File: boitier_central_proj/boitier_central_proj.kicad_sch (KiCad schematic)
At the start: 1 part, among them U1 XIAO-nRF52840-SMD

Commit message: PCB V1
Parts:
- added D1: 1N5819, Diode_THT:D_DO-41_SOD81_P10.16mm_Horizontal, symbol Diode:1N5819
- added D2: LED, LED_THT:LED_D5.0mm, symbol Device:LED
- added J1, J4: Conn_01x02_Pin, Connector_JST:JST_XH_B2B-XH-A_1x02_P2.50mm_Vertical, symbol Connector:Conn_01x02_Pin
- added J2: Conn_01x03_Pin, Connector_JST:JST_XH_B3B-XH-A_1x03_P2.50mm_Vertical, symbol Connector:Conn_01x03_Pin
- added Q1: IRLZ34N, Package_TO_SOT_THT:TO-220-3_Vertical, symbol Transistor_FET:IRLZ34N
- added R1, R2: 1k, Resistor_THT:R_Axial_DIN0204_L3.6mm_D1.6mm_P2.54mm_Vertical, symbol Device:R
- added S1, S2: JS102011SAQN, Button_Switch_SMD:SW_SPDT_CK_JS102011SAQN, symbol JS102011SAQN:JS102011SAQN
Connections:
- net leds_GND is gone; now on net GND: U1.13 (GND)
- net Arme_Selection: now reaches U1.1 (P0.02_A0_D0)
- net Arme_Selection: now also S2.2
- net 3V3: now reaches U1.12 (3V3)
- net 3V3: now also D1.1 (K), J1.2 (Pin_2), S2.1
- net moteur_c: now reaches U1.3 (P0.28_A2_D2)
- net moteur_c: now also R1.2
- net Out+ renamed BAT+
- net BAT+: now also D2.2 (A), S1.2
- net Out- renamed GND
- net GND: now also D2.1 (K), J2.2 (Pin_2), J4.2 (Pin_2), Q1.3 (S), R2.2, S1.1, S2.3
- net leds_5V renamed LEDS+
- net LEDS+: now also J2.3 (Pin_3)
- net leds_dig renamed LEDS_C
- net LEDS_C: now also J2.1 (Pin_1)
- new net: D1.2 (A), J1.1 (Pin_1), Q1.2 (D)
- new net: Q1.1 (G), R1.1, R2.1
- new net: J4.1 (Pin_1), S1.3
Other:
- note added: "Alimentation"
- note added: "Connection LEDs"
- note added: "Gestion Moteur"
- note added: "Selection Armes"

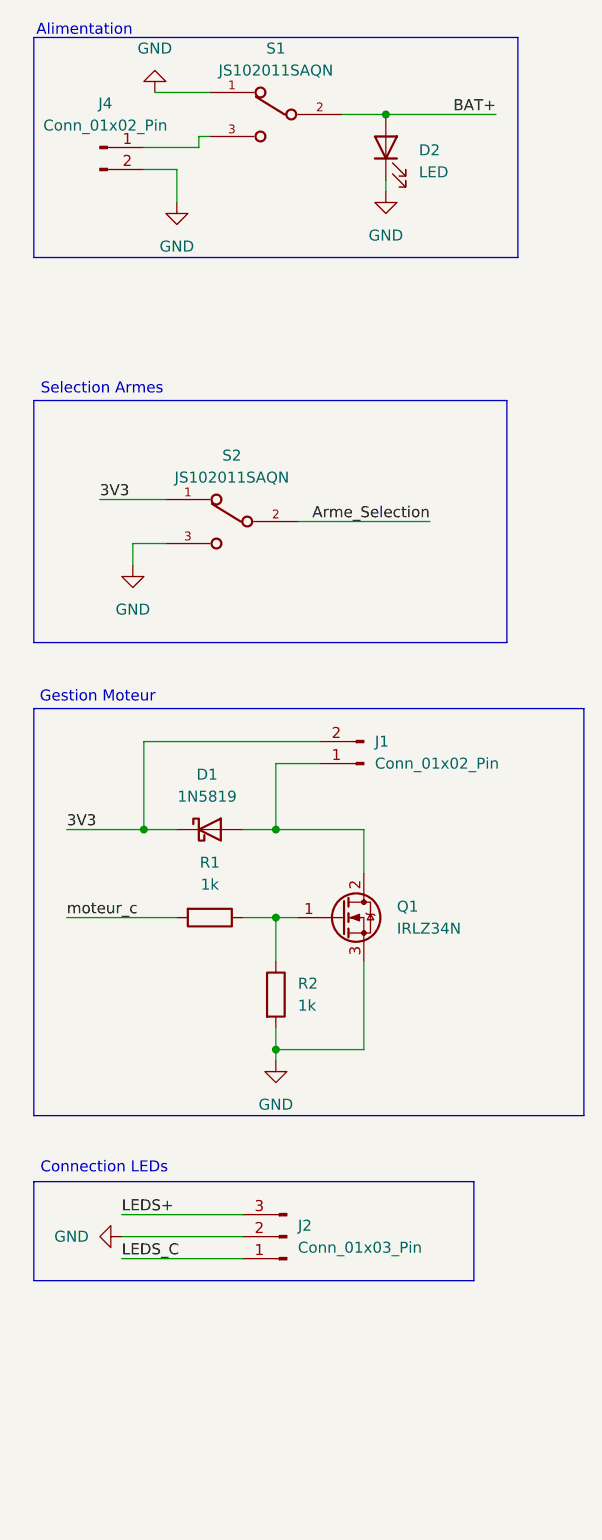
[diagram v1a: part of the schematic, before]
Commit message: Ajout du module TP4056 dans le schematic
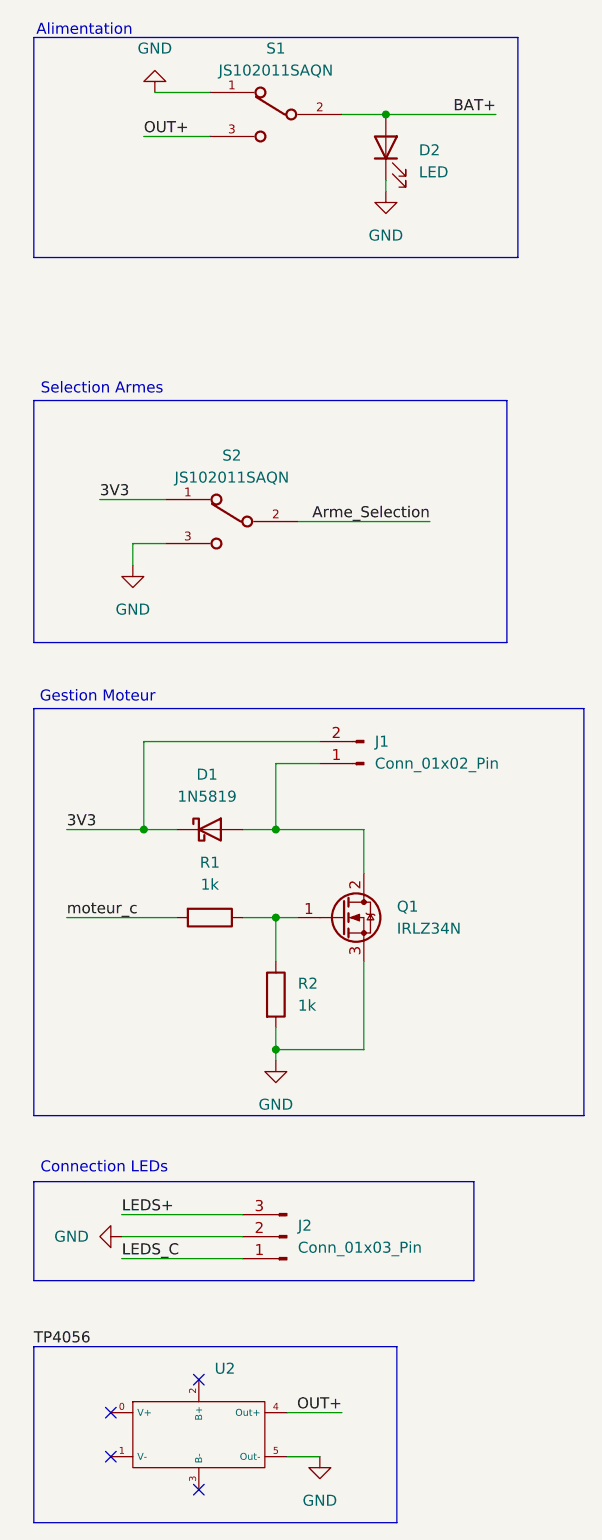
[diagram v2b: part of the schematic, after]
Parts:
- removed J4: Conn_01x02_Pin, Connector_JST:JST_XH_B2B-XH-A_1x02_P2.50mm_Vertical, symbol Connector:Conn_01x02_Pin
- added U2: ~, symbol TP4056_lib:TP4056_module
- S1, S2: footprint Button_Switch_SMD:SW_SPDT_CK_JS102011SAQN -> JS102011SAQN:SW_JS102011SAQN
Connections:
- net GND: now also U2.5 (Out-)
- net OUT+: now reaches S1.3
- net OUT+: now also U2.4 (Out+)
- no-connect marks 0 -> 4
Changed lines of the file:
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@@
 	(paper "A4")
+	(rectangle
+		(start 15.24 167.64)
+		(end 57.15 187.96)
+		(stroke
+			(width 0)
+			(type default)
+		)
+		(fill
+			(type none)
+		)
+	)
 	(rectangle
 		(start 15.24 148.59)
@@
 		(color 0 0 0 0)
 	)
+	(no_connect
+		(at 34.29 171.45)
+	)
+	(no_connect
+		(at 24.13 180.34)
+	)
+	(no_connect
+		(at 24.13 175.26)
+	)
+	(no_connect
+		(at 34.29 184.15)
+	)
 	(wire
 		(pts
@@
 	(wire
 		(pts
+			(xy 44.45 175.26) (xy 50.8 175.26)
+		)
+		(stroke
+			(width 0)
+			(type default)
+		)
+	)
+	(wire
+		(pts
 			(xy 48.26 100.33) (xy 43.18 100.33)
 		)
@@
 	(wire
 		(pts
-			(xy 34.29 27.94) (xy 35.56 27.94)
-		)
-		(stroke
-			(width 0)
-			(type default)
-		)
-	)
-	(wire
-		(pts
 			(xy 175.26 50.8) (xy 191.77 50.8)
 		)
@@
 	(wire
 		(pts
-			(xy 27.94 31.75) (xy 31.75 31.75)
-		)
-		(stroke
-			(width 0)
-			(type default)
-		)
-	)
-	(wire
-		(pts
 			(xy 53.34 133.35) (xy 43.18 133.35)
 		)
@@
 	(wire
 		(pts
+			(xy 44.45 180.34) (xy 48.26 180.34)
+		)
+		(stroke
+			(width 0)
+			(type default)
+		)
+	)
+	(wire
+		(pts
 			(xy 147.32 76.2) (xy 147.32 86.36)
 		)
@@
 	(wire
 		(pts
-			(xy 34.29 27.94) (xy 34.29 29.21)
-		)
-		(stroke
-			(width 0)
-			(type default)
-		)
-	)
-	(wire
-		(pts
 			(xy 115.57 50.8) (xy 133.35 50.8)
 		)
@@
 	(wire
 		(pts
-			(xy 34.29 29.21) (xy 27.94 29.21)
+			(xy 27.94 27.94) (xy 35.56 27.94)
 		)
 		(stroke
@@
 		(pts
 			(xy 26.67 74.93) (xy 26.67 77.47)
-		)
-		(stroke
-			(width 0)
-			(type default)
-		)
-	)
-	(wire
-		(pts
-			(xy 31.75 31.75) (xy 31.75 35.56)
 		)
 		(stroke
@@
 		)
 	)
+	(label "OUT+"
+		(at 50.8 175.26 180)
+		(effects
+			(font
+				(size 1.27 1.27)
+			)
+			(justify right bottom)
+		)
+	)
 	(label "BAT+"
 		(at 147.32 86.36 90)
@@
 		)
 	)
+	(label "TP4056"
+		(at 15.24 167.64 0)
+		(effects
+			(font
+				(size 1.27 1.27)
+			)
+			(justify left bottom)
+		)
+	)
 	(label "moteur_c"
 		(at 19.05 118.11 0)
@@
 			)
 			(justify right bottom)
+		)
+	)
+	(label "OUT+"
+		(at 27.94 27.94 0)
+		(effects
+			(font
+				(size 1.27 1.27)
+			)
+			(justify left bottom)
 		)
 	)
@@
 			)
 		)
-		(property "Footprint" "Button_Switch_SMD:SW_SPDT_CK_JS102011SAQN"
+		(property "Footprint" "JS102011SAQN:SW_JS102011SAQN"
 			(at 38.1 72.39 0)
 			(effects
@@
 			)
 		)
-		(property "Footprint" "Button_Switch_SMD:SW_SPDT_CK_JS102011SAQN"
+		(property "Footprint" "JS102011SAQN:SW_JS102011SAQN"
 			(at 43.18 25.4 0)
 			(effects
@@
 				(path "/6fcf47c7-8342-4a1b-bafb-526012532a3f"
 					(reference "S1")
+					(unit 1)
+				)
+			)
+		)
+	)
+	(symbol
+		(lib_id "power:GND")
+		(at 48.26 180.34 0)
+		(unit 1)
+		(exclude_from_sim no)
+		(in_bom yes)
+		(on_board yes)
+		(dnp no)
+		(fields_autoplaced yes)
+		(property "Reference" "#PWR09"
+			(at 48.26 186.69 0)
+			(effects
+				(font
+					(size 1.27 1.27)
+				)
+				(hide yes)
+			)
+		)
+		(property "Value" "GND"
+			(at 48.26 185.42 0)
+			(effects
+				(font
+					(size 1.27 1.27)
+				)
+			)
+		)
+		(property "Footprint" ""
+			(at 48.26 180.34 0)
+			(effects
+				(font
+					(size 1.27 1.27)
+				)
+				(hide yes)
+			)
+		)
+		(property "Datasheet" ""
+			(at 48.26 180.34 0)
+			(effects
+				(font
+					(size 1.27 1.27)
+				)
+				(hide yes)
+			)
+		)
+		(property "Description" "Power symbol creates a global label with name \"GND\" , ground"
+			(at 48.26 180.34 0)
+			(effects
+				(font
+					(size 1.27 1.27)
+				)
+				(hide yes)
+			)
+		)
+		(pin "1"
+		)
+		(instances
+			(project ""
+				(path "/6fcf47c7-8342-4a1b-bafb-526012532a3f"
+					(reference "#PWR09")
 					(unit 1)
 				)
@@
 	(symbol
 		(lib_id "power:GND")
-		(at 31.75 35.56 0)
-		(unit 1)
-		(exclude_from_sim no)
-		(in_bom yes)
-		(on_board yes)
-		(dnp no)
-		(fields_autoplaced yes)
-		(property "Reference" "#PWR07"
-			(at 31.75 41.91 0)
-			(effects
-				(font
-					(size 1.27 1.27)
-				)
-				(hide yes)
-			)
-		)
-		(property "Value" "GND"
-			(at 31.75 40.64 0)
-			(effects
-				(font
-					(size 1.27 1.27)
-				)
-			)
-		)
-		(property "Footprint" ""
-			(at 31.75 35.56 0)
-			(effects
-				(font
-					(size 1.27 1.27)
-				)
-				(hide yes)
-			)
-		)
-		(property "Datasheet" ""
-			(at 31.75 35.56 0)
-			(effects
-				(font
-					(size 1.27 1.27)
-				)
-				(hide yes)
-			)
-		)
-		(property "Description" "Power symbol creates a global label with name \"GND\" , ground"
-			(at 31.75 35.56 0)
-			(effects
-				(font
-					(size 1.27 1.27)
-				)
-				(hide yes)
-			)
-		)
-		(pin "1"
-		)
-		(instances
-			(project ""
-				(path "/6fcf47c7-8342-4a1b-bafb-526012532a3f"
-					(reference "#PWR07")
-					(unit 1)
-				)
-			)
-		)
-	)
-	(symbol
-		(lib_id "power:GND")
 		(at 25.4 154.94 270)
 		(unit 1)
@@
 	)
 	(symbol
-		(lib_id "Connector:Conn_01x02_Pin")
-		(at 22.86 29.21 0)
+		(lib_id "TP4056_lib:TP4056_module")
+		(at 41.91 173.99 0)
 		(unit 1)
 		(exclude_from_sim no)
@@
 		(dnp no)
 		(fields_autoplaced yes)
-		(property "Reference" "J4"
-			(at 23.495 24.13 0)
-			(effects
-				(font
-					(size 1.27 1.27)
-				)
-			)
-		)
-		(property "Value" "Conn_01x02_Pin"
-			(at 23.495 26.67 0)
-			(effects
-				(font
-					(size 1.27 1.27)
-				)
-			)
-		)
-		(property "Footprint" "Connector_JST:JST_XH_B2B-XH-A_1x02_P2.50mm_Vertical"
-			(at 22.86 29.21 0)
-			(effects
-				(font
-					(size 1.27 1.27)
-				)
-				(hide yes)
-			)
-		)
-		(property "Datasheet" "~"
-			(at 22.86 29.21 0)
-			(effects
-				(font
-					(size 1.27 1.27)
-				)
-				(hide yes)
-			)
-		)
-		(property "Description" "Generic connector, single row, 01x02, script generated"
-			(at 22.86 29.21 0)
-			(effects
-				(font
-					(size 1.27 1.27)
-				)
-				(hide yes)
-			)
+		(property "Reference" "U2"
+			(at 36.1101 170.18 0)
+			(effects
+				(font
+					(size 1.27 1.27)
+				)
+				(justify left)
+			)
+		)
+		(property "Value" "~"
+			(at 36.1101 172.72 0)
+			(effects
+				(font
+					(size 1.27 1.27)
+				)
+				(justify left)
+			)
+		)
+		(property "Footprint" ""
+			(at 41.91 173.99 0)
+			(effects
+				(font
+					(size 1.27 1.27)
+				)
+				(hide yes)
+			)
+		)
+		(property "Datasheet" ""
+			(at 41.91 173.99 0)
+			(effects
+				(font
+					(size 1.27 1.27)
+				)
+				(hide yes)
+			)
+		)
+		(property "Description" ""
+			(at 41.91 173.99 0)
+			(effects
+				(font
+					(size 1.27 1.27)
+				)
+				(hide yes)
+			)
+		)
+		(pin "3"
+		)
+		(pin "2"
+		)
+		(pin "4"
+		)
+		(pin "5"
 		)
 		(pin "1"
 		)
-		(pin "2"
+		(pin "0"
 		)
 		(instances
-			(project "boitier_central_proj"
+			(project ""
 				(path "/6fcf47c7-8342-4a1b-bafb-526012532a3f"
-					(reference "J4")
+					(reference "U2")
 					(unit 1)
 				)

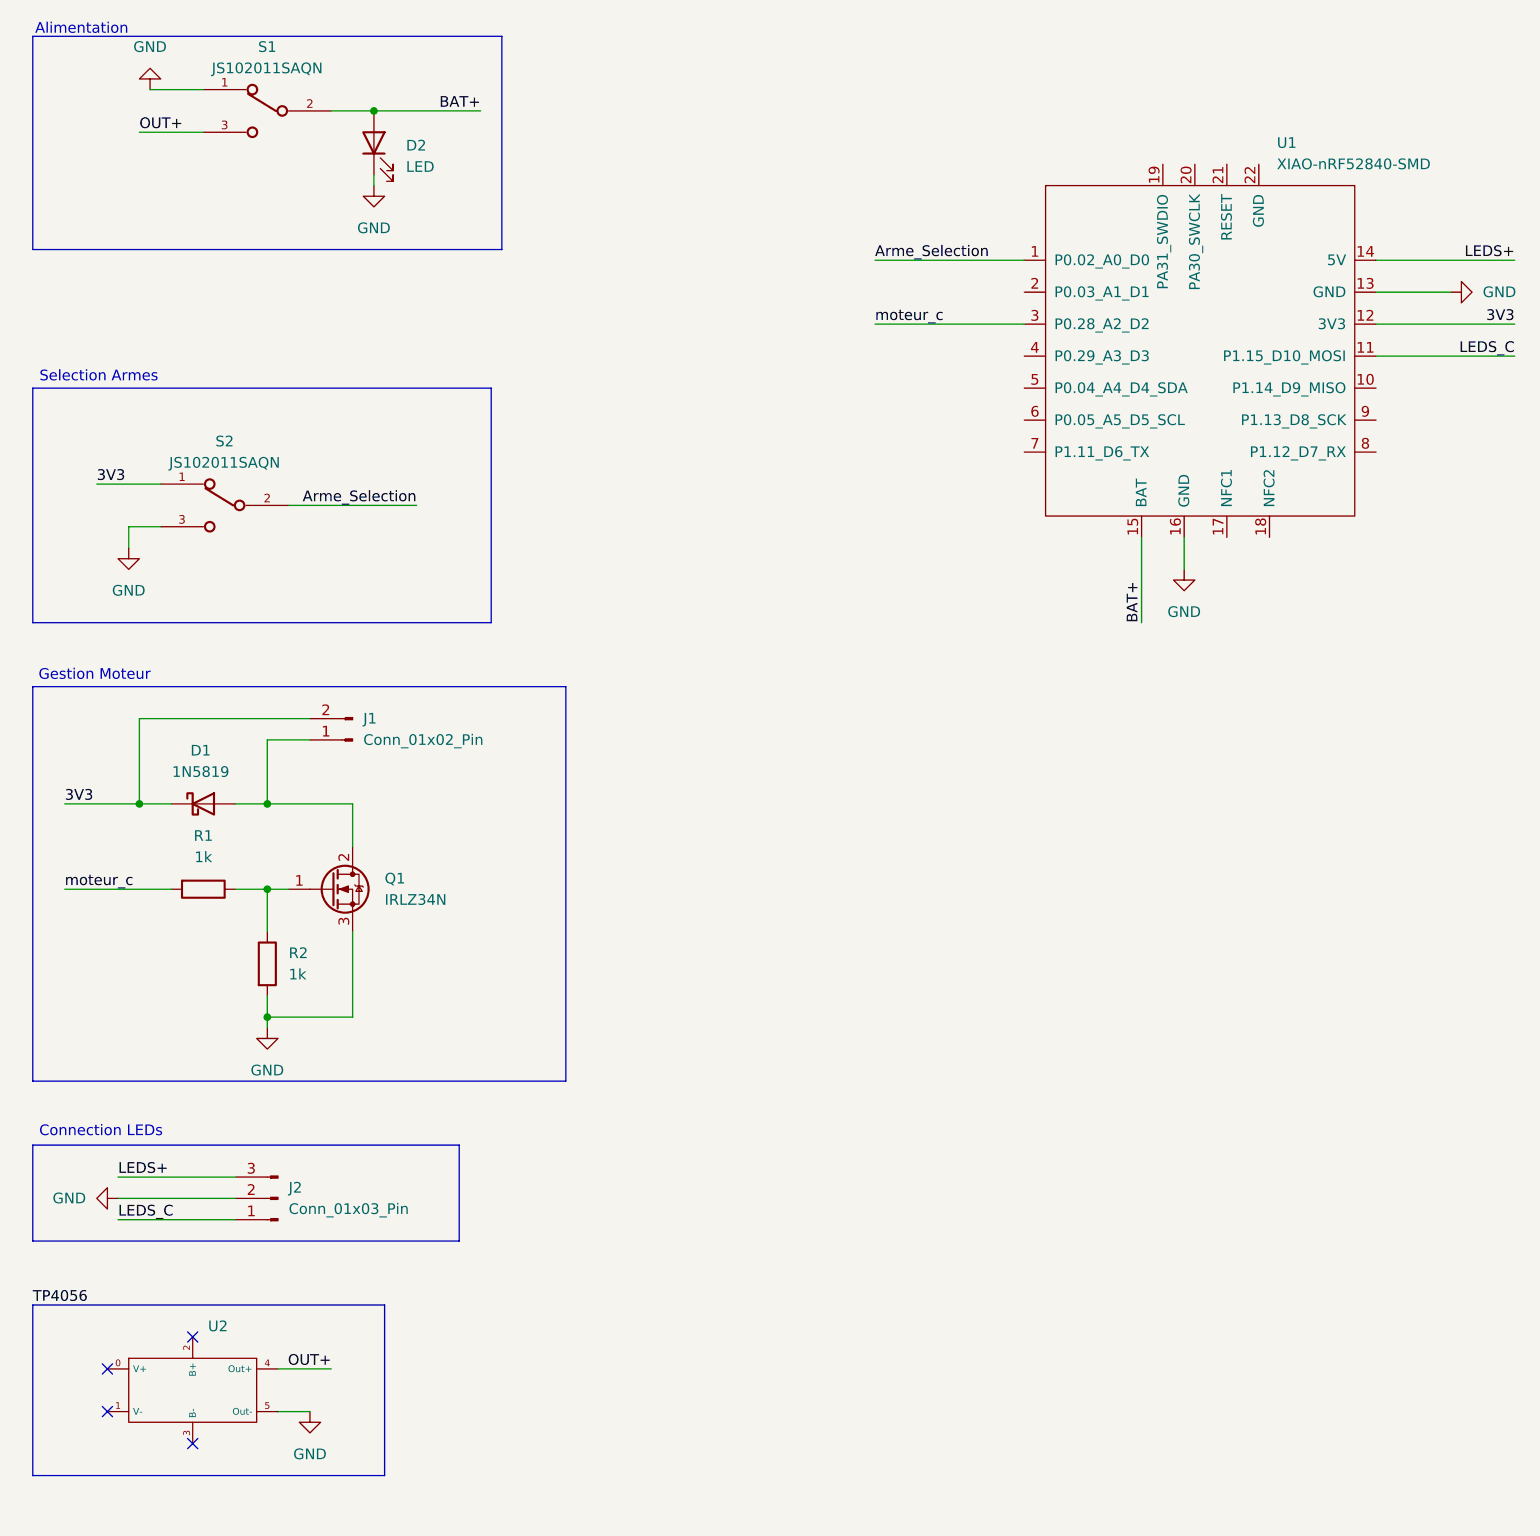
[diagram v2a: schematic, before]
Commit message: Ajout du 3d duseeduiino et du tp4056 + ajout des trous
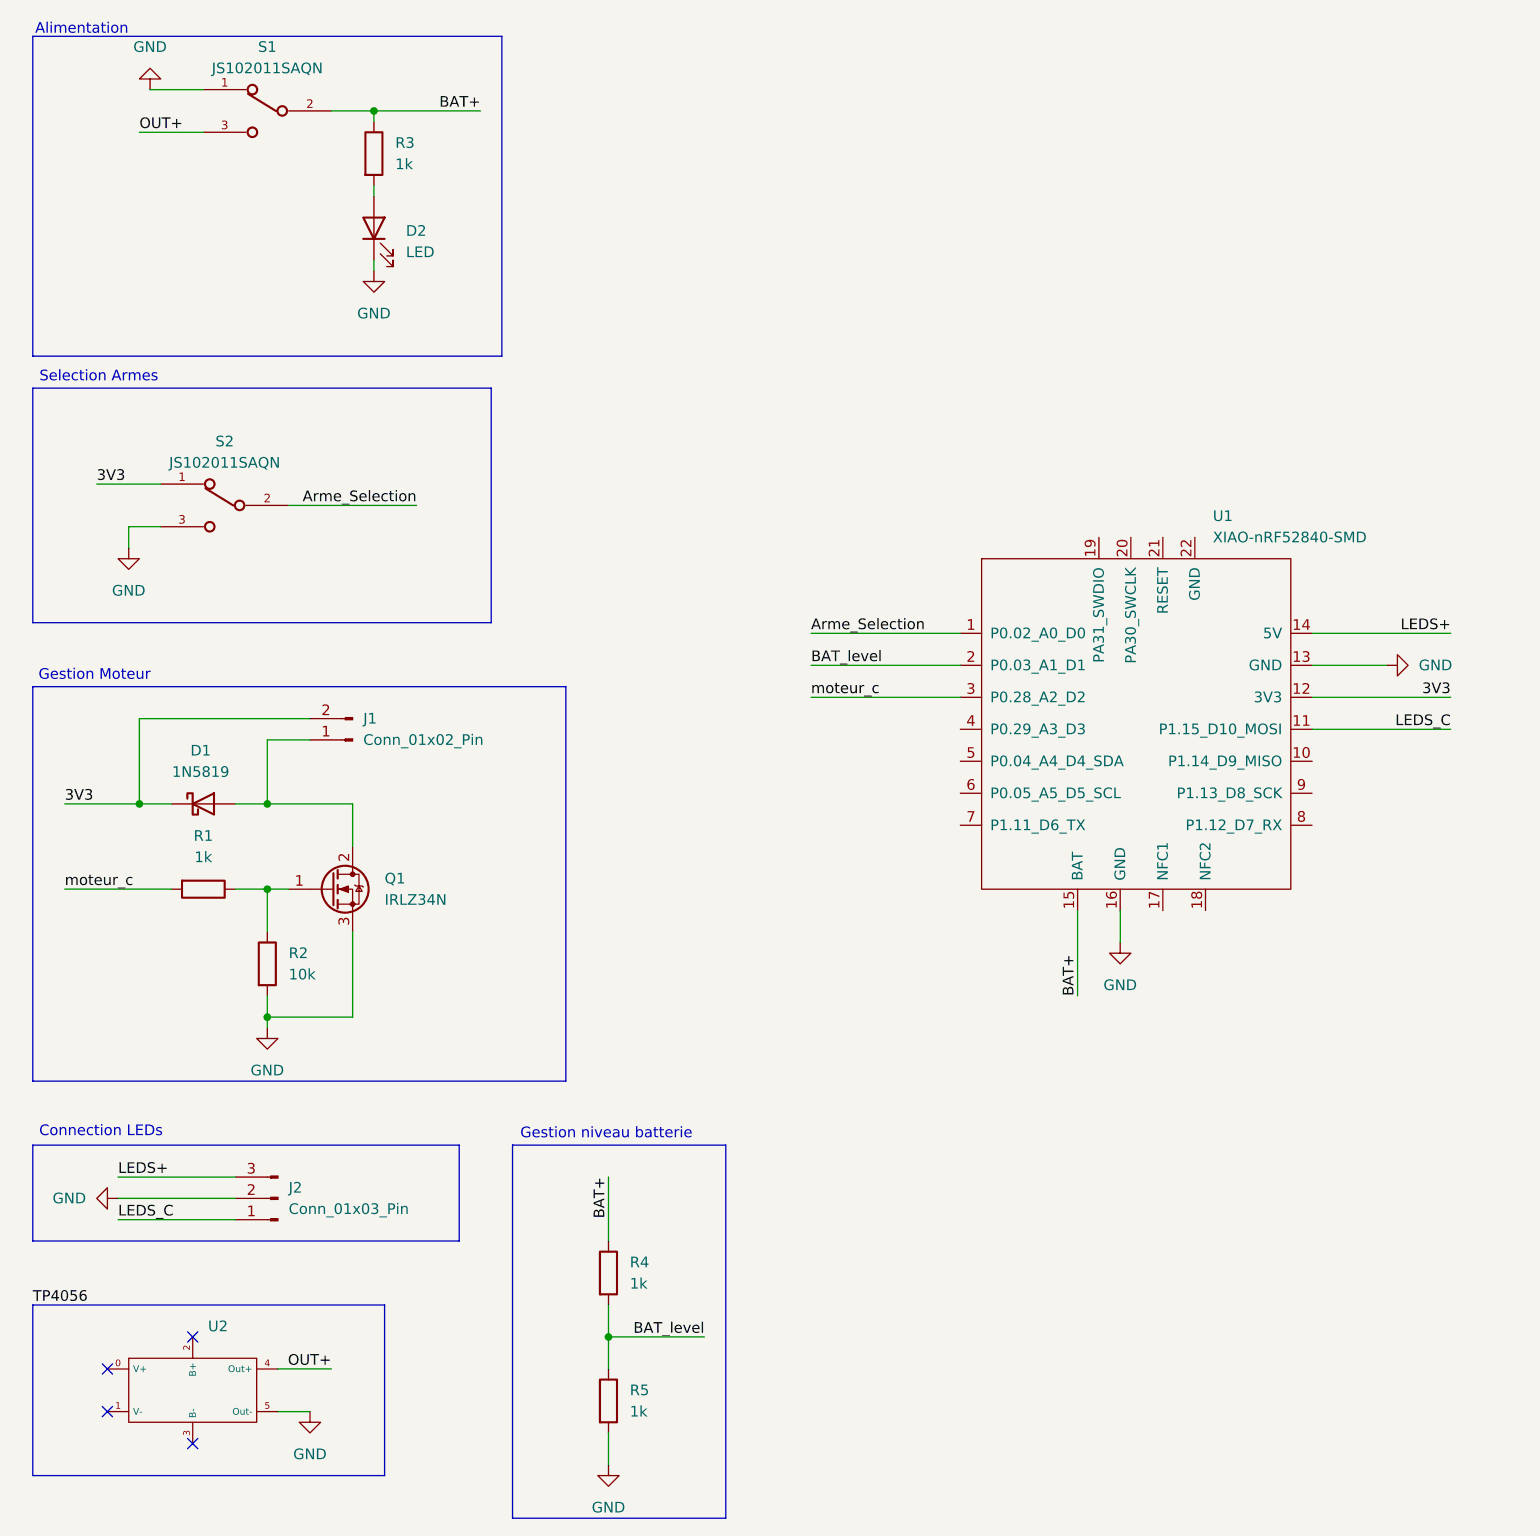
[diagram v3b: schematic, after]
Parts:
- added R3, R4, R5: 1k, Resistor_THT:R_Axial_DIN0204_L3.6mm_D1.6mm_P2.54mm_Vertical, symbol Device:R
- R2: value 1k -> 10k
- S1, S2: footprint JS102011SAQN:SW_JS102011SAQN -> Button_Switch_SMD:SW_SPDT_CK_JS102011SAQN
- U2: footprint (none) -> TP4056:TP4056
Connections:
- net BAT+: now also R3.1, R4.1; no longer D2.2 (A)
- net GND: now also R5.2
- net BAT_level: now reaches U1.2 (P0.03_A1_D1)
- net BAT_level: now also R4.2, R5.1
- new net: D2.2 (A), R3.2
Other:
- note added: "Gestion niveau batterie"
- moved on the sheet: D2, U1
